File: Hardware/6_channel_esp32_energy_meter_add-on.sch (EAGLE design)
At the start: 105 parts, among them IC1 ATM90E32AS, IC2 ATM90E32AS, J16 PINHD-1X19, J4 TMM-103-01-T-D-SM, J5 PINHD1X1-SM1X01_SM, J6 PINHD1X1-SM1X01_SM, J7 TMM-103-01-T-D-SM, J8 PINHD1X1-SM1X01_SM, U1 ESP32-DEVKITC-32D, Y1 16.384MHz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

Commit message: v1.3 rev2
– Added voltage divider on ground for voltage channel 2
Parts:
- R14: value 1K -> 100
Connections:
- net IO12: no longer J4.10
- net IO2: no longer J4.11
- net IO27: now also J4.11
- net IO35: now also J4.10

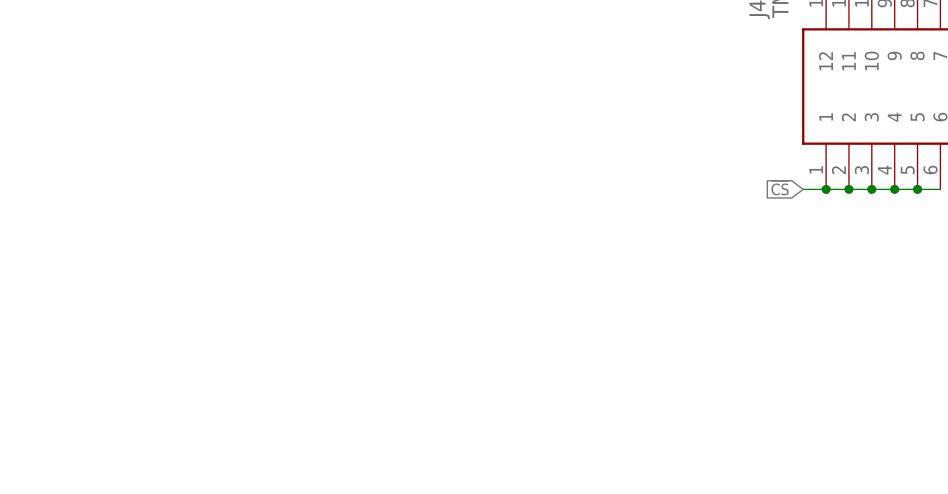
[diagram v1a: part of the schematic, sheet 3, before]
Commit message: v1.4
- Added optional micro-hdmi connection to connect the current transformer remote board. This allows for all 6 current transformer connections to connect to a remote pcb, which then connects to the main board via 1 micro-hdmi cable. Instead of 6 wires coming out of the meter, there can now be 1.
- Added current transformer remote pcb
- Removed JP8-JP11 and connected all voltage channels together for each ATM90E32
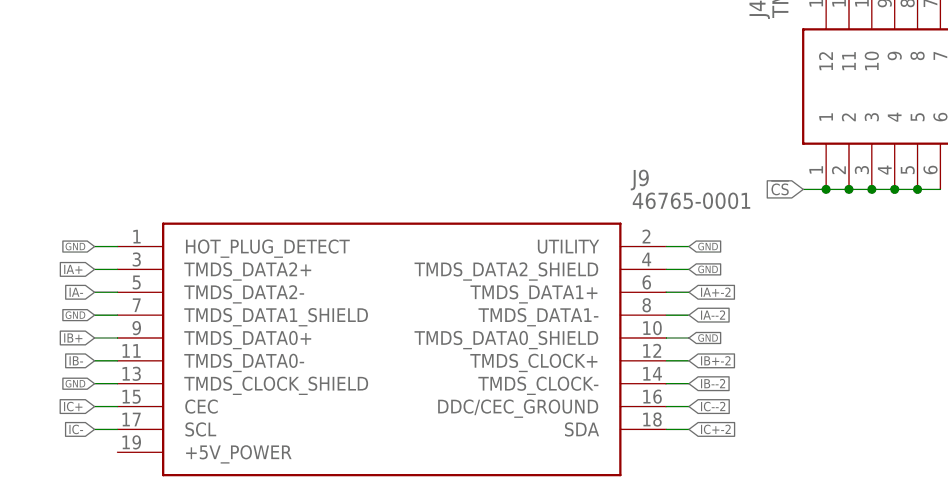
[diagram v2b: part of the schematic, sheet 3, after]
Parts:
- removed JP10, JP11, JP8, JP9: JUMPER-SMT_3_NO_SILK, SparkFun-Jumpers:JUMPER-SMT_3_NO_SILK
- added J9: 46765-0001, 46765-0001:46765-0001
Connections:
- removed net V2N: IC1.V2N, JP9.3
- removed net V2N-2: IC2.V2N, JP11.3
- removed net V2P: IC1.V2P, JP8.3
- removed net V2P-2: IC2.V2P, JP10.3
- removed net V3N: IC1.V3N, JP9.1
- removed net V3N-2: IC2.V3N, JP11.1
- removed net V3P: IC1.V3P, JP8.1
- removed net V3P-2: IC2.V3P, JP10.1
- net GND: now also J9.HOT_PLUG_DETECT, J9.TMDS_CLOCK_SHIELD, J9.TMDS_DATA0_SHIELD, J9.TMDS_DATA1_SHIELD, J9.TMDS_DATA2_SHIELD, J9.UTILITY
- net IA+: now also J9.TMDS_DATA2+
- net IA+-2: now also J9.TMDS_DATA1+
- net IA-: now also J9.TMDS_DATA2-
- net IA--2: now also J9.TMDS_DATA1-
- net IB+: now also J9.TMDS_DATA0+
- net IB+-2: now also J9.TMDS_CLOCK+
- net IB-: now also J9.TMDS_DATA0-
- net IB--2: now also J9.TMDS_CLOCK-
- net IC+: now also J9.CEC
- net IC+-2: now also J9.SDA
- net IC-: now also J9.SCL
- net IC--2: now also J9.DDC/CEC_GROUND
- net VAN: now also IC1.V2N, IC1.V3N; no longer JP9.2
- net VAN2: now also IC2.V2N, IC2.V3N; no longer JP11.2
- net VAP: now also IC1.V2P, IC1.V3P; no longer JP8.2
- net VAP2: now also IC2.V2P, IC2.V3P; no longer JP10.2

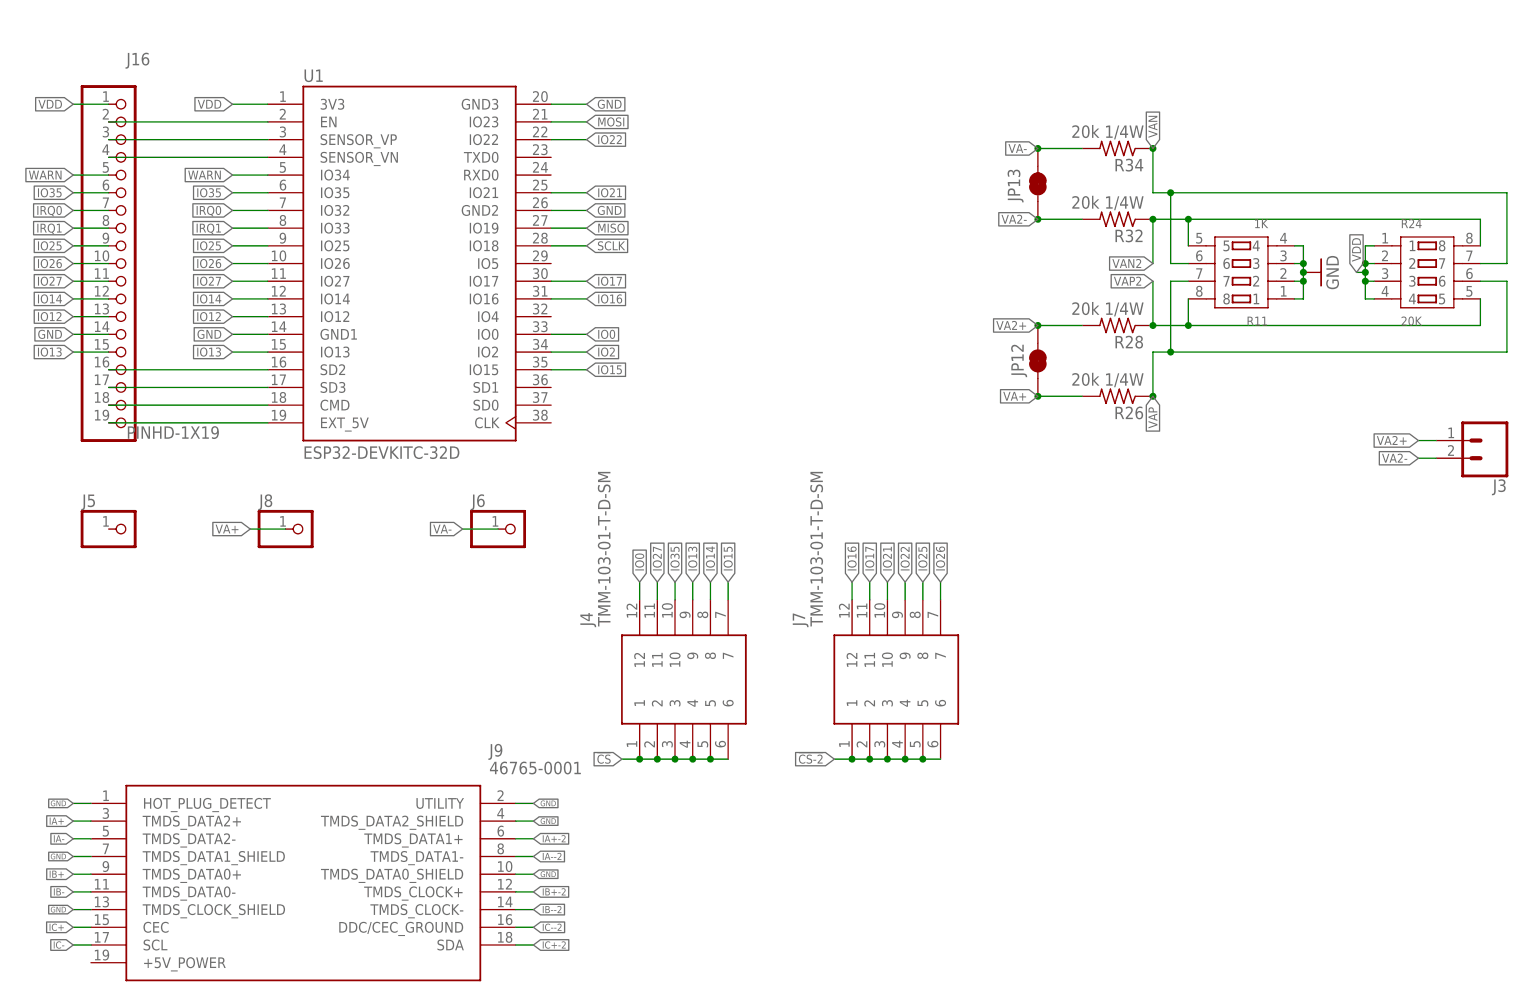
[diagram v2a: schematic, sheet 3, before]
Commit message: Updated Eagle files to v1.4 rev1
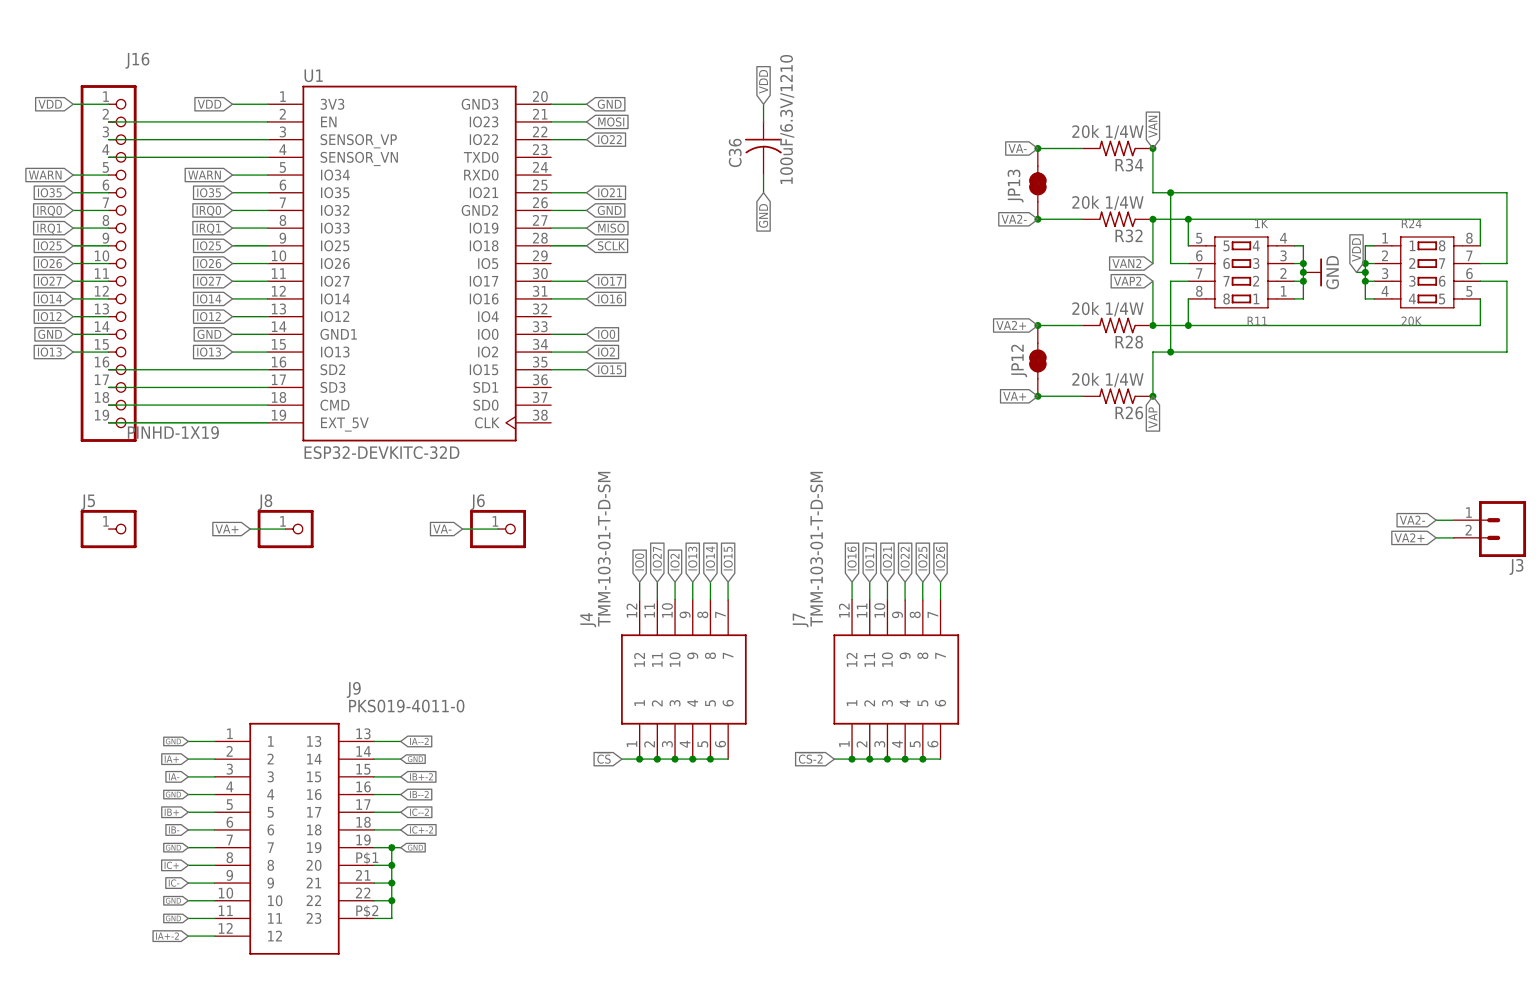
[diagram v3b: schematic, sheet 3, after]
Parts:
- added C36: 100uF/6.3V/1210, rcl:C-USC1210
- J3: device SparkFun-Connectors:CONN_02 -> SparkFun-Connectors:CONN_023.5MM
- J9: value 46765-0001 -> PKS019-4011-0; device 46765-0001:46765-0001 -> SamacSys_Parts:PKS019-4011-0
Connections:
- net GND: now also C36.2, J9.1, J9.10, J9.11, J9.14, J9.19, J9.20, J9.21, J9.22, J9.23, J9.4, J9.7; no longer J9.HOT_PLUG_DETECT, J9.TMDS_CLOCK_SHIELD, J9.TMDS_DATA0_SHIELD, J9.TMDS_DATA1_SHIELD, J9.TMDS_DATA2_SHIELD, J9.UTILITY
- net IA+: now also J9.2; no longer J9.TMDS_DATA2+
- net IA+-2: now also J9.12; no longer J9.TMDS_DATA1+
- net IA-: now also J9.3; no longer J9.TMDS_DATA2-
- net IA--2: now also J9.13; no longer J9.TMDS_DATA1-
- net IB+: now also J9.5; no longer J9.TMDS_DATA0+
- net IB+-2: now also J9.15; no longer J9.TMDS_CLOCK+
- net IB-: now also J9.6; no longer J9.TMDS_DATA0-
- net IB--2: now also J9.16; no longer J9.TMDS_CLOCK-
- net IC+: now also J9.8; no longer J9.CEC
- net IC+-2: now also J9.18; no longer J9.SDA
- net IC-: now also J9.9; no longer J9.SCL
- net IC--2: now also J9.17; no longer J9.DDC/CEC_GROUND
- net IO2: now also J4.10
- net IO35: no longer J4.10
- net VA2+: now also J3.2; no longer J3.1
- net VA2-: now also J3.1; no longer J3.2
- net VDD: now also C36.1
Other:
- moved on the sheet: J3
